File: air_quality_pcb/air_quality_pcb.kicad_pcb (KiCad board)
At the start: 2 copper layers, 3 parts, among them IC1 SCD41-D-R2, IC2 SGP41-D-R4, U1 XIAO-ESP32-C6

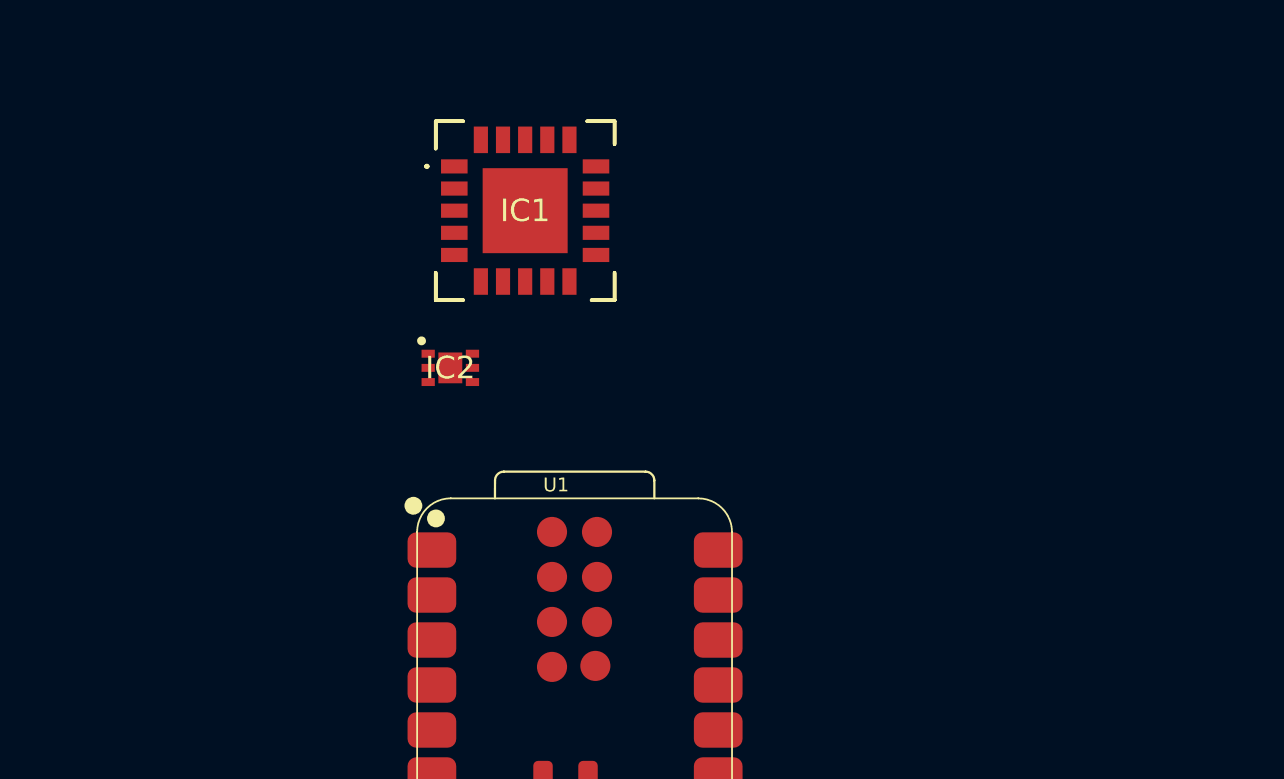
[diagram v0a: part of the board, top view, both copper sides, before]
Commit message: added sensors and display example
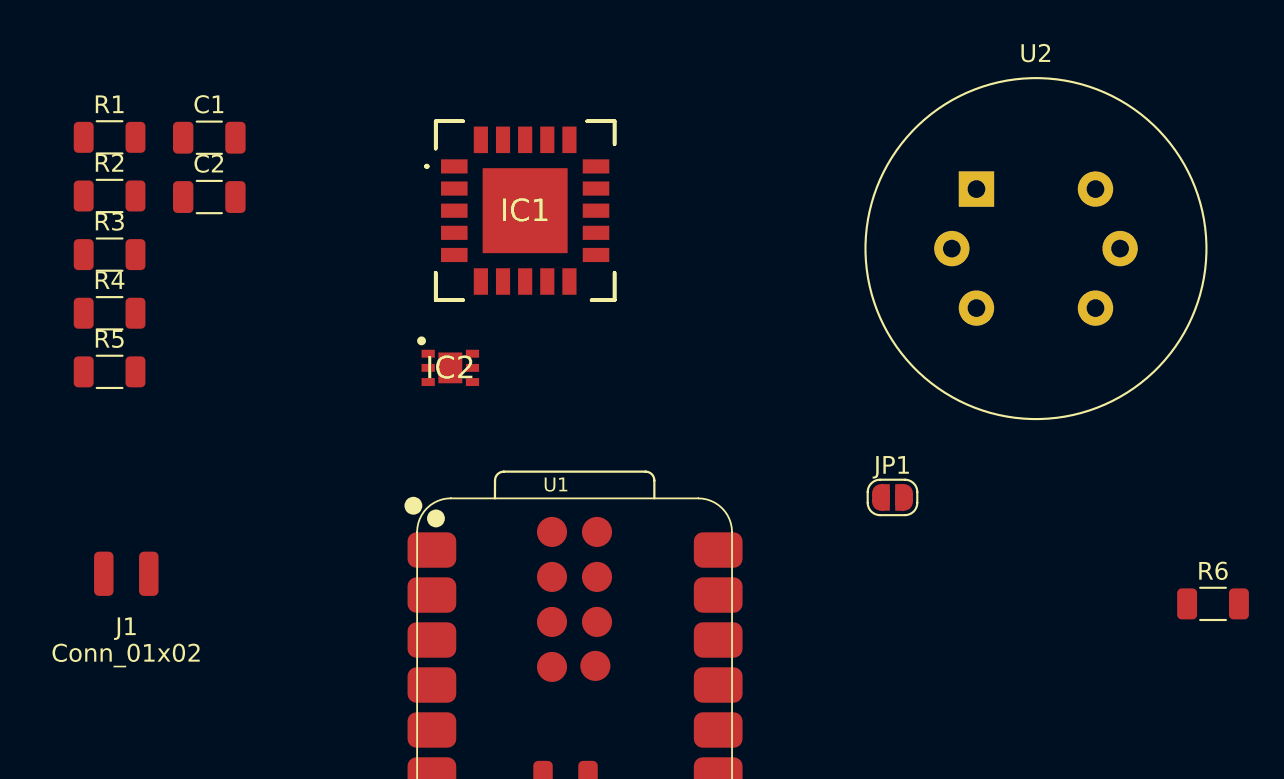
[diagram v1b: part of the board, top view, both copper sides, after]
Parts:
- added C1: 1uF, Capacitor_SMD:C_1206_3216Metric, F.Cu at (132.3, 71.1)
- added C2: 1uF, Capacitor_SMD:C_1206_3216Metric, F.Cu at (132.3, 74.4)
- added J1: Conn_01x02, project_extras:BATT_connector, F.Cu at (127.6, 99.2)
- added JP1: Jumper_2_Open, Jumper:SolderJumper-2_P1.3mm_Open_RoundedPad1.0x1.5mm, F.Cu at (170.8, 91.4)
- added R1: 10k, Resistor_SMD:R_1206_3216Metric, F.Cu at (126.6, 71.1)
- added R2: 10k, Resistor_SMD:R_1206_3216Metric, F.Cu at (126.6, 74.4)
- added R3: 10k, Resistor_SMD:R_1206_3216Metric, F.Cu at (126.6, 77.7)
- added R4: 10k, Resistor_SMD:R_1206_3216Metric, F.Cu at (126.6, 81.0)
- added R5: 4.7, Resistor_SMD:R_1206_3216Metric, F.Cu at (126.6, 84.3)
- added R6: 4.7k, Resistor_SMD:R_1206_3216Metric, F.Cu at (188.9, 97.4)
- added U2: MQ-6, Sensor:MQ-6, F.Cu at (175.6, 74.0)
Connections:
- IC1 pad 10: unconnected-(IC1-SDA-Pad10) -> SDA
- IC1 pad 19: unconnected-(IC1-VDDH-Pad19) -> +3V3
- IC1 pad 20: unconnected-(IC1-GND_2-Pad20) -> GND
- IC1 pad 21: unconnected-(IC1-GND_3-Pad21) -> GND
- IC1 pad 6: unconnected-(IC1-GND_1-Pad6) -> GND
- IC1 pad 9: unconnected-(IC1-SCL-Pad9) -> SCL
- IC2 pad 1: unconnected-(IC2-VDD-Pad1) -> Net-(IC2-VDD)
- IC2 pad 2: unconnected-(IC2-VSS-Pad2) -> GND
- IC2 pad 3: unconnected-(IC2-SDA-Pad3) -> SDA
- IC2 pad 4: unconnected-(IC2-N/A-Pad4) -> GND
- IC2 pad 5: unconnected-(IC2-VDDH-Pad5) -> +3V3
- IC2 pad 6: unconnected-(IC2-SCL-Pad6) -> SCL
- IC2 pad 7: unconnected-(IC2-EP-Pad7) -> GND
- U1 pad 1: unconnected-(U1-GPIO2_A0_D0-Pad1) -> A0
- U1 pad 12: unconnected-(U1-3V3-Pad12) -> +3V3
- U1 pad 13: unconnected-(U1-GND-Pad13) -> GND
- U1 pad 14: unconnected-(U1-VBUS-Pad14) -> +5V
- U1 pad 15: unconnected-(U1-bat+-Pad15) -> +BATT
- U1 pad 16: unconnected-(U1-bat--Pad16) -> Net-(JP1-A)
- U1 pad 5: unconnected-(U1-GPIO6_D4_SDA-Pad5) -> SDA
- U1 pad 6: unconnected-(U1-GPIO7_D5_SCL-Pad6) -> SCL

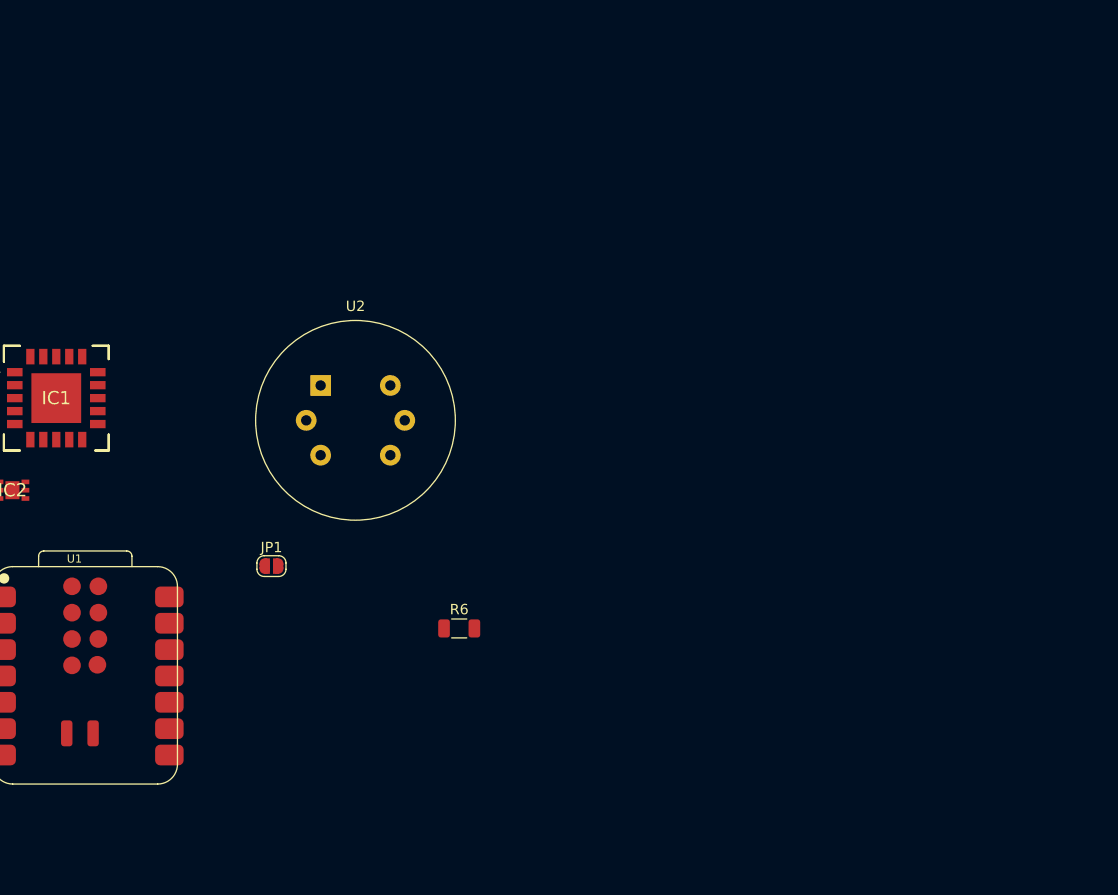
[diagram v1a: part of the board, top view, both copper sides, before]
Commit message: added mq7 sensor and display connector
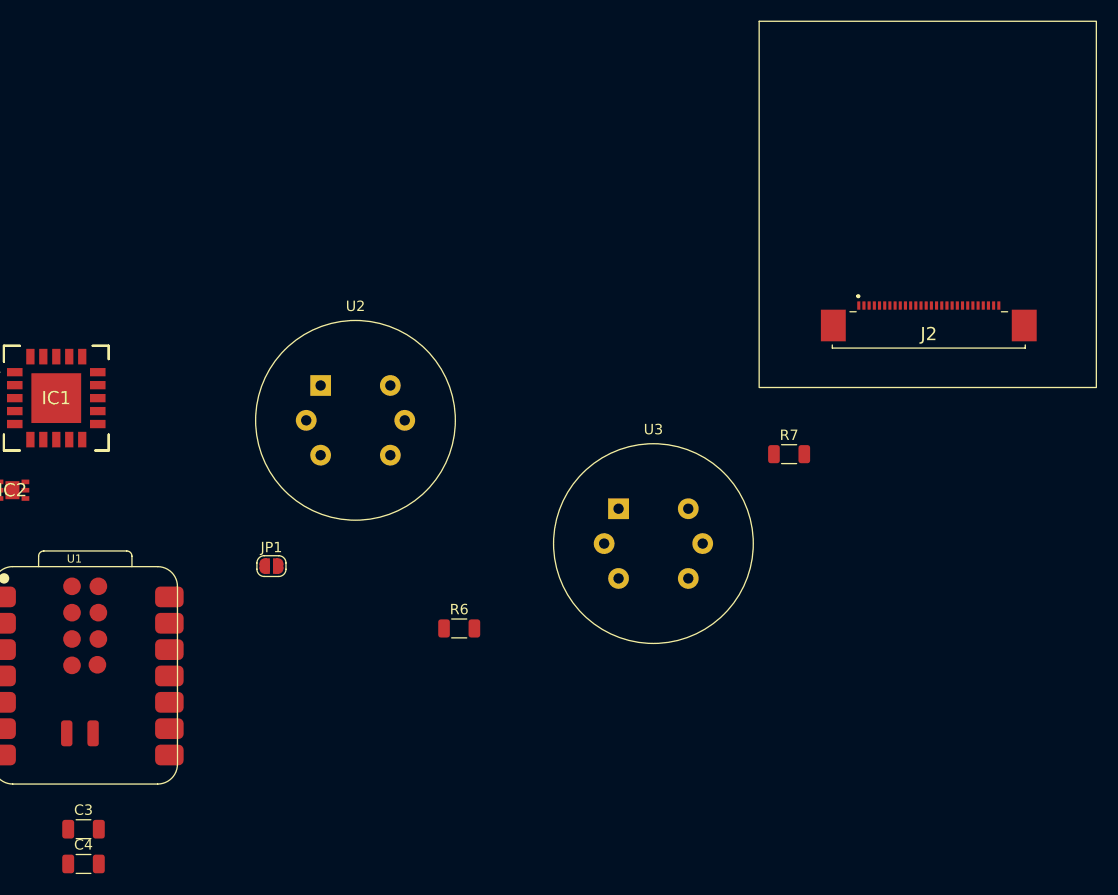
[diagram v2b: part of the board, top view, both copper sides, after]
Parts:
- added C3: 1uF, Capacitor_SMD:C_1206_3216Metric, F.Cu at (152.7, 116.8)
- added C4: 0.1uF, Capacitor_SMD:C_1206_3216Metric, F.Cu at (152.7, 120.1)
- added J2: 52435-2871, project_extras:display_connector, F.Cu at (234.2, 69.0)
- added R7: 4.7k, Resistor_SMD:R_1206_3216Metric, F.Cu at (220.7, 80.6)
- added U3: MQ-6, Sensor:MQ-6, F.Cu at (204.3, 85.9)
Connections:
- U1 pad 10: unconnected-(U1-GPIO9_D9_MISO-Pad10) -> SDOX
- U1 pad 11: unconnected-(U1-GPIO10_D10_MOSI-Pad11) -> SDAX
- U1 pad 2: unconnected-(U1-GPIO3_A1_D1-Pad2) -> A1
- U1 pad 3: unconnected-(U1-GPIO4_A2_D2-Pad3) -> CSX
- U1 pad 4: unconnected-(U1-GPIO5_A3_D3-Pad4) -> RESX
- U1 pad 7: unconnected-(U1-GPIO21_D6_TX-Pad7) -> TE
- U1 pad 8: unconnected-(U1-GPIO20_D7_RX-Pad8) -> WRX
- U1 pad 9: unconnected-(U1-GPIO8_D8_SCK-Pad9) -> DCX

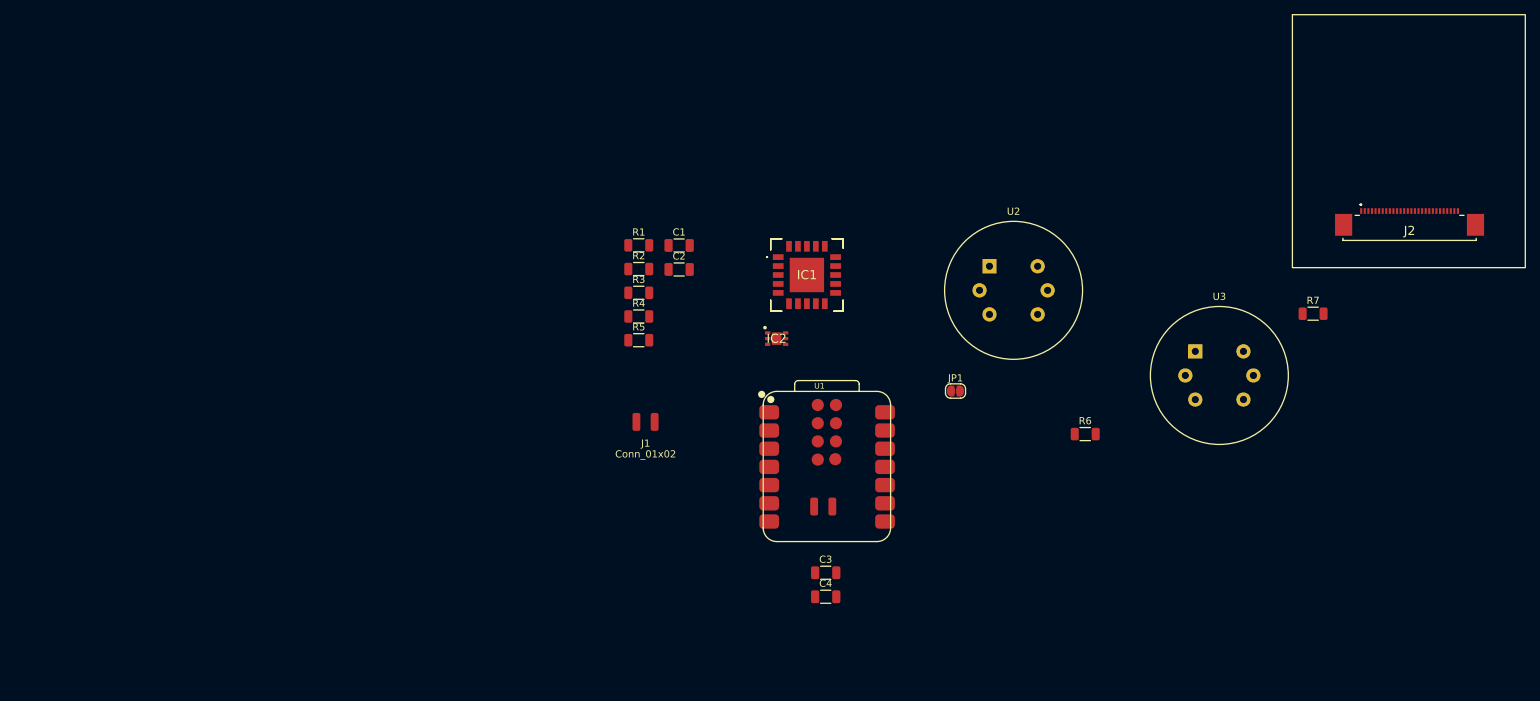
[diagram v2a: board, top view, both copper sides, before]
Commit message: finished routing and added more decoupling caps
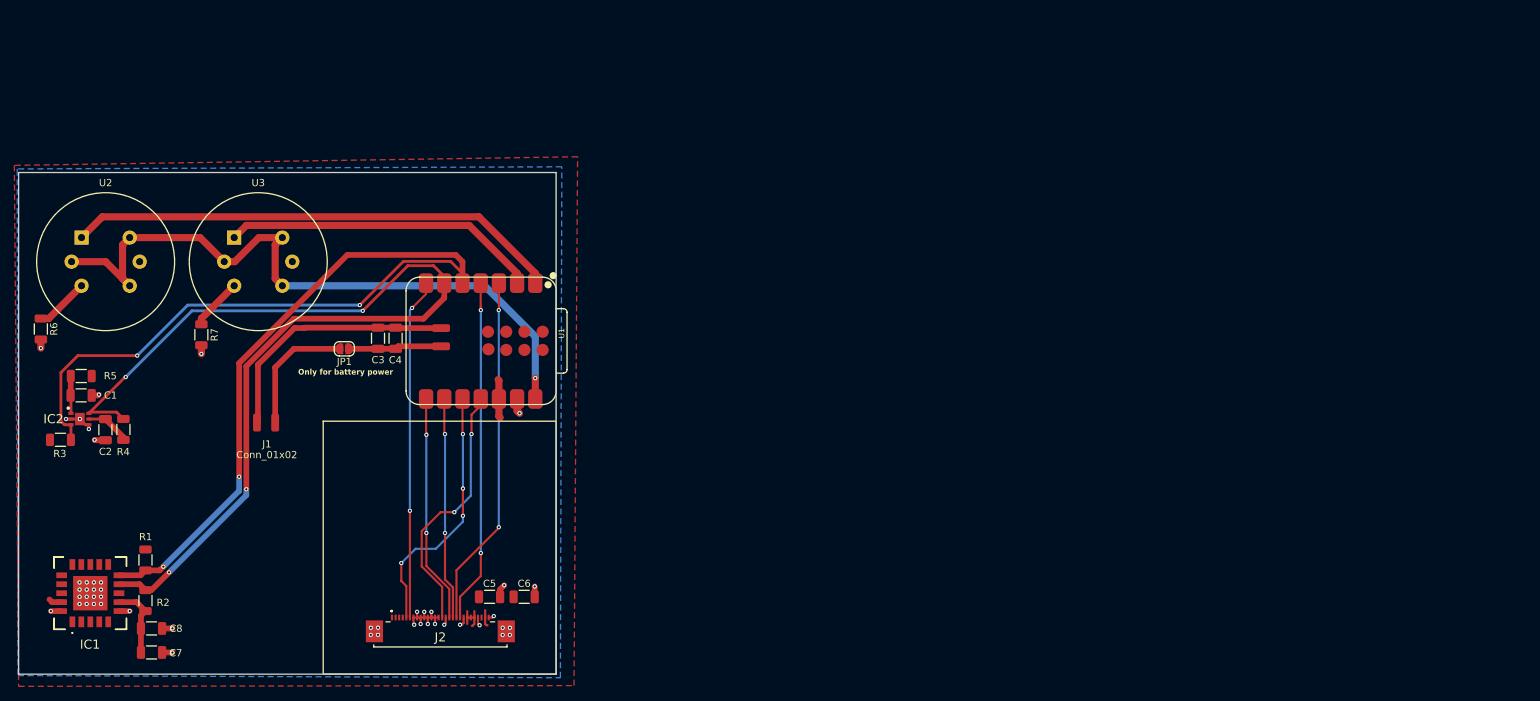
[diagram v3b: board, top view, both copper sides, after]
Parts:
- added C5: 0.1uF, Capacitor_SMD:C_1206_3216Metric, F.Cu at (105.8, 120.1)
- added C6: 1uF, Capacitor_SMD:C_1206_3216Metric, F.Cu at (110.6, 120.1)
- added C7: 0.1uF, Capacitor_SMD:C_1206_3216Metric, F.Cu at (58.6, 127.9)
- added C8: 1uF, Capacitor_SMD:C_1206_3216Metric, F.Cu at (58.6, 124.5)
- moved R7 155.2 mm to (65.6, 83.5), turned to -90 degrees
- moved J2 146.7 mm to (99.0, 125.8)
- moved R6 146.5 mm to (43.2, 82.7), turned to -90 degrees
- moved U3 135.1 mm to (70.2, 70.0)
- moved U2 126.8 mm to (48.9, 70.0)
- moved IC1 109.4 mm to (50.1, 119.6), turned to 90 degrees
- moved IC2 97.9 mm to (48.6, 95.3)
- moved C1 86.0 mm to (48.8, 92.0)
- moved JP1 85.5 mm to (85.5, 85.5), turned to 180 degrees
- moved R3 83.3 mm to (45.9, 98.2)
- moved C2 83.1 mm to (52.2, 96.8), turned to -90 degrees
- moved R2 82.9 mm to (57.8, 120.6), turned to 90 degrees
- moved R1 81.6 mm to (57.8, 115.0), turned to -90 degrees
- moved R5 78.0 mm to (48.8, 89.3), turned to 180 degrees
- moved R4 73.6 mm to (54.7, 96.8), turned to 90 degrees
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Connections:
- IC1 pad 7: unconnected-(IC1-VDD-Pad7) -> +3V3
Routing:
- net SDA: track 0.00 -> 155.3 mm, vias 0 -> 4
- net SCL: track 0.00 -> 140.2 mm, vias 0 -> 4
- net +5V: track 0.00 -> 95.6 mm, vias 0 -> 1
- net A0: track 0.00 -> 69.2 mm
- net CSX: track 0.00 -> 49.1 mm, vias 0 -> 2
- net RESX: track 0.00 -> 47.9 mm, vias 0 -> 2
- net TE: track 0.00 -> 47.6 mm, vias 0 -> 2
- net A1: track 0.00 -> 44.3 mm
- net SDAX: track 0.00 -> 36.2 mm, vias 0 -> 2
- net SDOX: track 0.00 -> 36.0 mm, vias 0 -> 4
- net +BATT: track 0.00 -> 35.9 mm
- net GND: track 0.00 -> 34.5 mm, vias 0 -> 49
- net WRX: track 0.00 -> 31.8 mm, vias 0 -> 2
- net +3V3: track 0.00 -> 31.2 mm
- net DCX: track 0.00 -> 31.0 mm, vias 0 -> 2
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- added copper zone on F.Cu, net +3V3
- added copper zone on B.Cu, net GND
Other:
- board outline added: 75 x 70 mm
- board text added: "Only for battery power"
